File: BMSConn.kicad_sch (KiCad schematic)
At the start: 6 parts, among them J2 CONN HEADER VERT 2POS 1.5MM, J3 CONN HEADER VERT 2POS 1.5MM, T1 PULSE XFMR 15UH 1 OHM FOR PLC

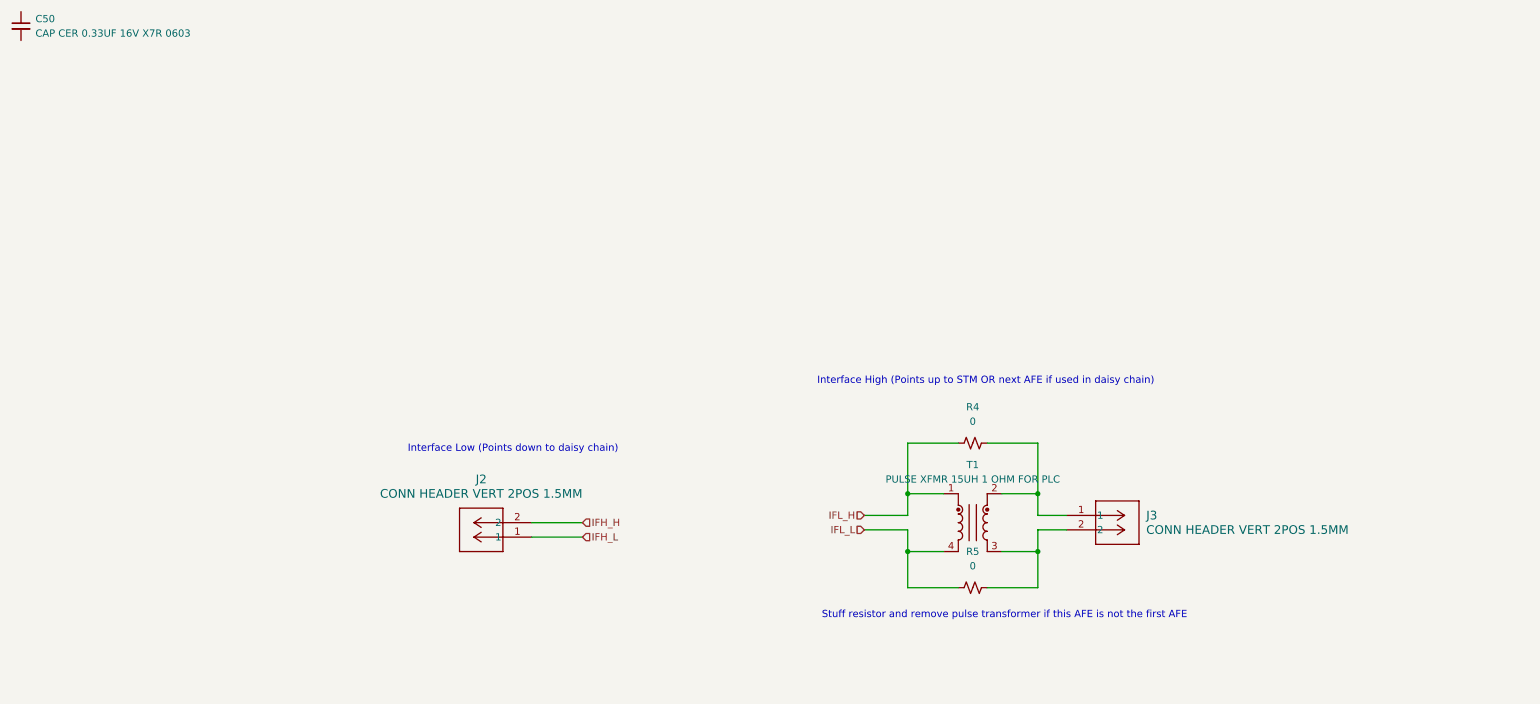
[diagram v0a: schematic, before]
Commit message: cleaned up schematic
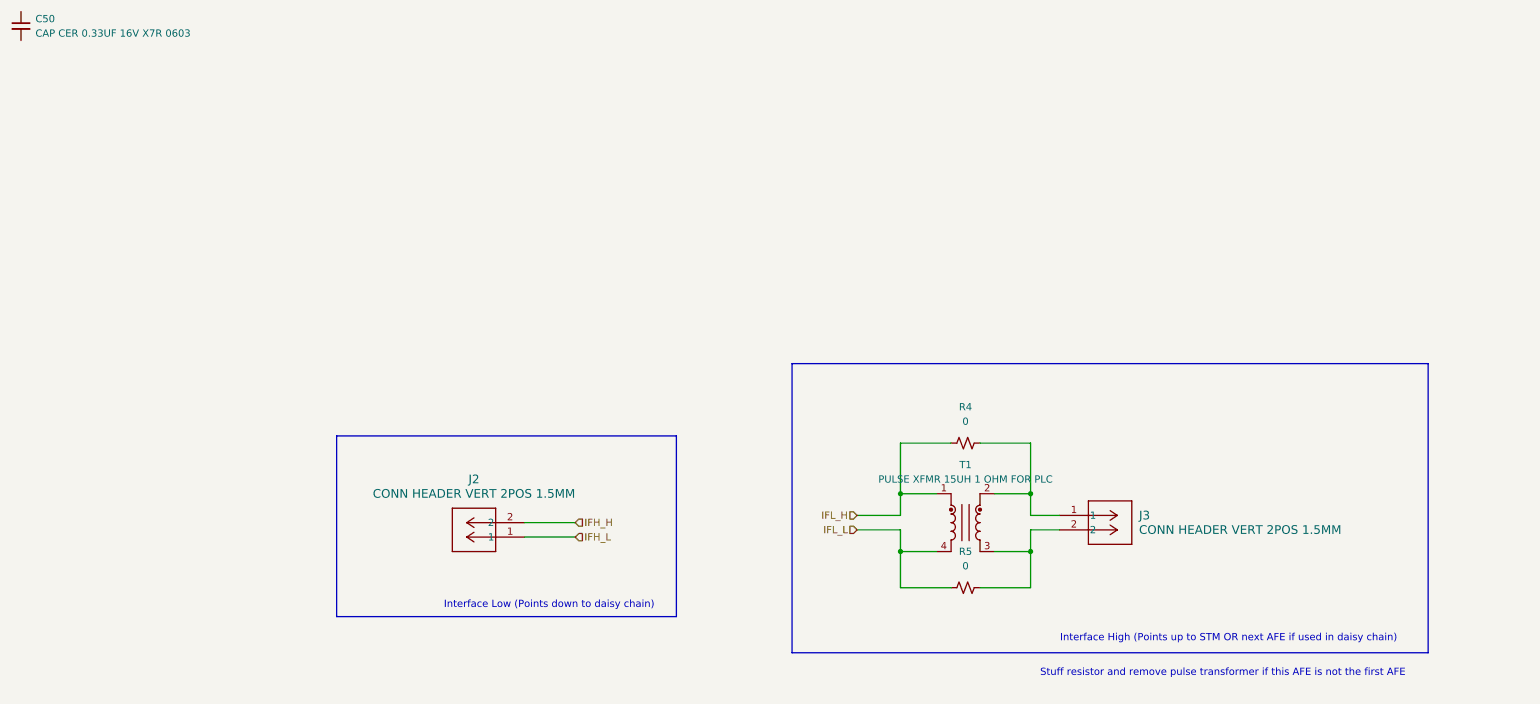
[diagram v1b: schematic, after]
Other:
- moved on the sheet: J2, J3, R4, R5, T1

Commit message: added damping resistor on other side of pulse transformer
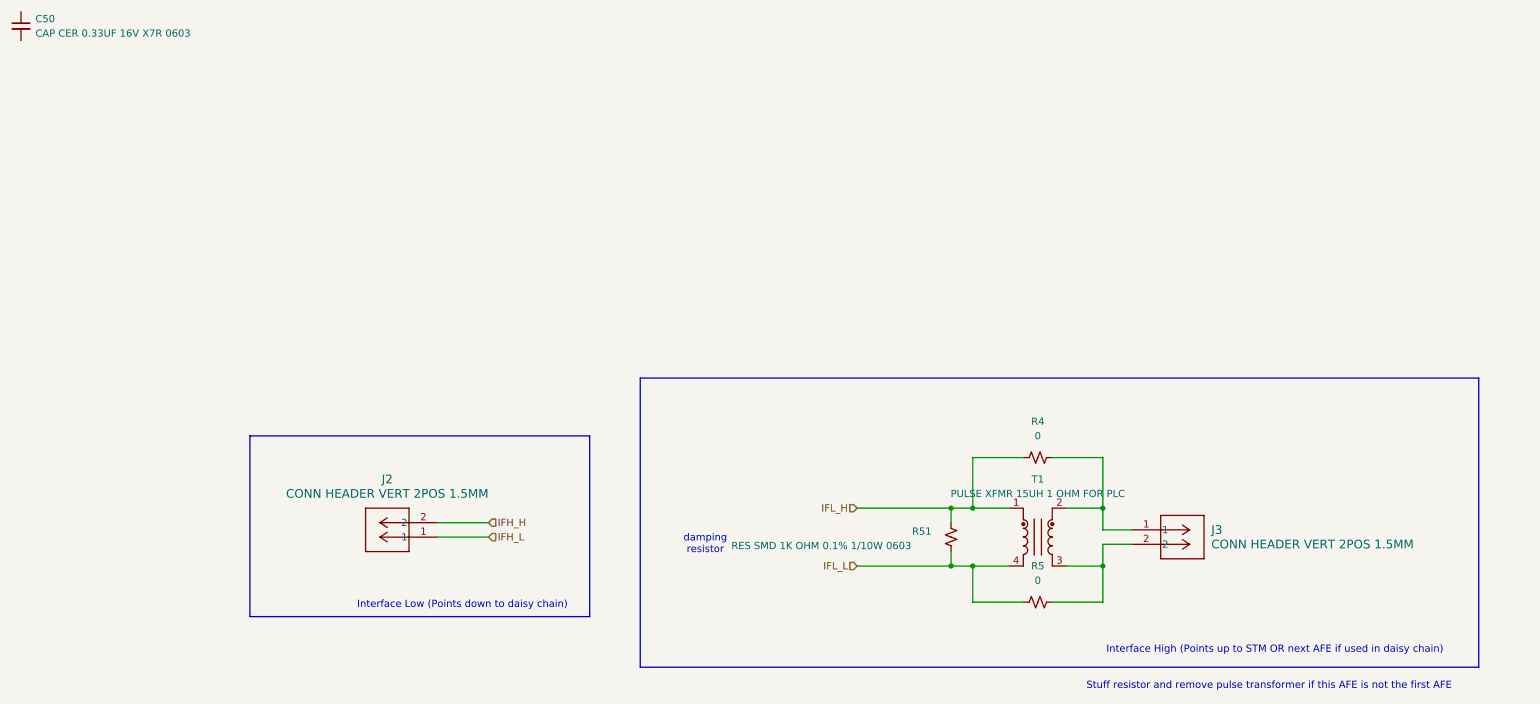
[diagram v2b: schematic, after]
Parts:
- added R51: RES SMD 1K OHM 0.1% 1/10W 0603, Resistor_SMD:R_0603_1608Metric, symbol Device:R_Small_US
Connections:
- net IFL_H: now also R51.2
- net IFL_L: now also R51.1
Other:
- note added: "damping resistor"
- moved on the sheet: J2, J3, R4, R5, T1

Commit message: fixed capacitor values
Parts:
- R4, R5: footprint (none) -> Resistor_SMD:R_0603_1608Metric
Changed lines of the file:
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@@
 			)
 		)
-		(property "Footprint" ""
+		(property "Footprint" "Resistor_SMD:R_0603_1608Metric"
 			(at 180.34 104.14 0)
 			(hide yes)
@@
 			)
 		)
-		(property "Footprint" ""
+		(property "Footprint" "Resistor_SMD:R_0603_1608Metric"
 			(at 180.34 78.74 0)
 			(hide yes)

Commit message: minor changes
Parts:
- removed C50: CAP CER 0.33UF 16V X7R 0603, Capacitor_SMD:C_0603_1608Metric, symbol Device:C_Small
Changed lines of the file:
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@@
-	)
-	(symbol
-		(lib_id "Device:C_Small")
-		(at 1.6891 2.9211 0)
-		(unit 1)
-		(body_style 1)
-		(exclude_from_sim no)
-		(in_bom yes)
-		(on_board yes)
-		(in_pos_files yes)
-		(dnp no)
-		(fields_autoplaced yes)
-		(property "Reference" "C50"
-			(at 4.2291 1.6573 0)
-			(show_name no)
-			(do_not_autoplace no)
-			(effects
-				(font
-					(size 1.27 1.27)
-				)
-				(justify left)
-			)
-		)
-		(property "Value" "CAP CER 0.33UF 16V X7R 0603"
-			(at 4.2291 4.1973 0)
-			(show_name no)
-			(do_not_autoplace no)
-			(effects
-				(font
-					(size 1.27 1.27)
-				)
-				(justify left)
-			)
-		)
-		(property "Footprint" "Capacitor_SMD:C_0603_1608Metric"
-			(at 1.6891 2.9211 0)
-			(hide yes)
-			(show_name no)
-			(do_not_autoplace no)
-			(effects
-				(font
-					(size 1.27 1.27)
-				)
-			)
-		)
-		(property "Datasheet" "https://www.digikey.ca/en/products/detail/samsung-electro-mechanics/CL10B334KO8NNNC/3887706"
-			(at 1.6891 2.9211 0)
-			(hide yes)
-			(show_name no)
-			(do_not_autoplace no)
-			(effects
-				(font
-					(size 1.27 1.27)
-				)
-			)
-		)
-		(property "Description" "0.33 µF ±10% 16V Ceramic Capacitor X7R 0603 (1608 Metric)"
-			(at 1.6891 2.9211 0)
-			(hide yes)
-			(show_name no)
-			(do_not_autoplace no)
-			(effects
-				(font
-					(size 1.27 1.27)
-				)
-			)
-		)
-		(pin "2"
-		)
-		(pin "1"
-		)
-		(instances
-			(project "bms-afe"
-				(path "/226a23e7-09bb-40bc-b53a-ec42a6b7cc90/6d53ec20-967d-414a-950d-119f66d4f6c2"
-					(reference "C50")
-					(unit 1)
-				)
-			)
-		)
 	)
 	(symbol
